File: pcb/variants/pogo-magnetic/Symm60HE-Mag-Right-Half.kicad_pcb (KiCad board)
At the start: 2 copper layers, 158.9 x 107.8 mm, 123 parts

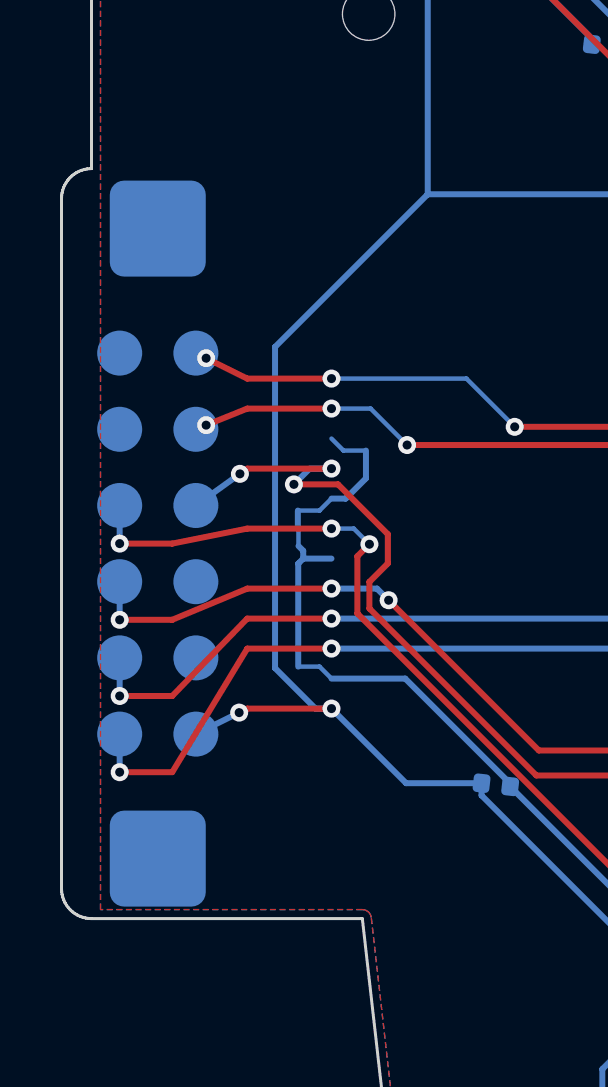
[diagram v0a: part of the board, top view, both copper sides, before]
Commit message: Survey the stocked magnetic pogo parts at twelve contacts and up
No manufacturer catalogue publishes a magnetic part above eight contacts, but
the ODM market does: single row on 2.54 mm goes to twenty, and dual row on
2.54 mm offers 8, 10, 12, 14 and 20 poles. Record the families with their
contact spans, since span is what decides whether a part fits the kernel.

A single-row twelve-contact part spans 27.94 mm, so about a 40 mm housing on a
47 mm module. The 2 x 6 dual row spans 12.70 mm on the 32 mm module this
variant already builds, which is why it wins despite the harder fanout.

Sixteen was tried: PER_ROW = 8 generates and routes but leaves three clearance
flags on the left half instead of two, so the crossing is the anchor geometry
rather than a shortage of slots, and it costs 5 mm of module length for four
spare grounds. Reverted to twelve.

Also move footprint generation into tools/make_mag_pogo_footprints.py so the
ICD constants drive the land pattern, and generalise the verifier's ground
count so either width checks.

Co-Authored-By: Claude Opus 5 <noreply@anthropic.com>
Claude-Session: https://claude.ai/code/session_01CRkZ4zVz5Mq7Fa3C5HAmii
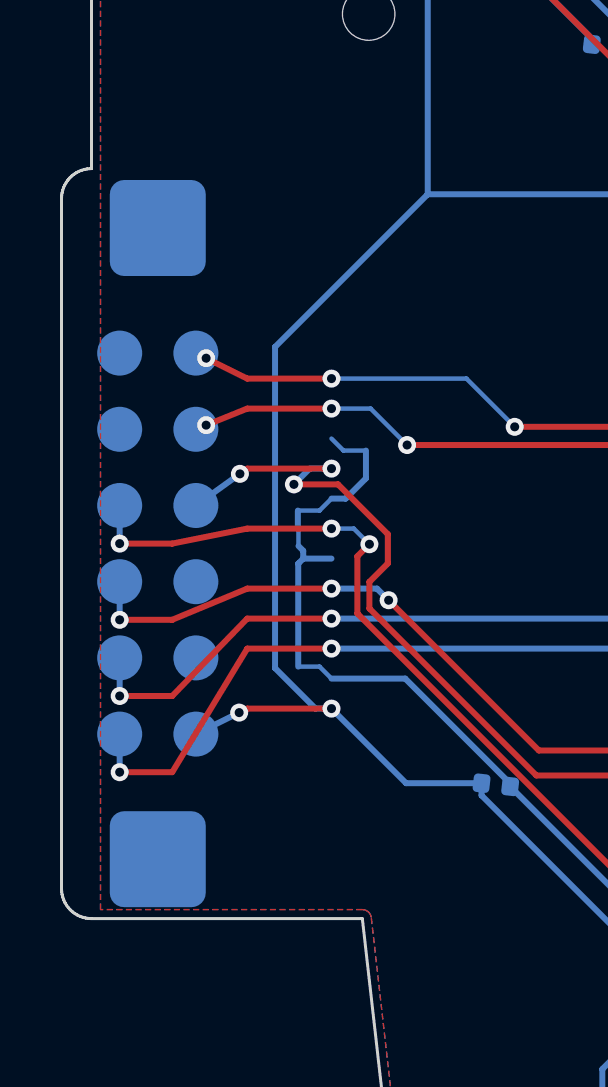
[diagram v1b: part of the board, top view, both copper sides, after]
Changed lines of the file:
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@@
 		(at 154.418 56 90)
 		(layer "B.Cu")
-		(descr "Magnetic pogo target half mating with MagPogo_2x6_P254_Spring. Built to ICD MAGPOGO-2x6-P254; confirm against the supplier drawing.")
+		(descr "Magnetic pogo target half mating with MagPogo_2x6_P254_Spring. Built to ICD MAGPOGO; confirm against the supplier drawing.")
 		(tags "magnetic pogo target 2x6 2.54mm")
 		(property
@@
 		(attr smd)
 		(fp_rect
-			(start -12.5 -4.5)
-			(end 12.5 4.5)
+			(start -12.52 -4.5)
+			(end 12.52 4.5)
 			(stroke
 				(width 0.12)
@@
 		)
 		(fp_rect
-			(start -13.0 -5.0)
-			(end 13.0 5.0)
+			(start -13.02 -5.0)
+			(end 13.02 5.0)
 			(stroke
 				(width 0.05)
@@
 		)
 		(fp_line
-			(start -12.5 -4.5)
-			(end 12.5 -4.5)
+			(start -12.52 -4.5)
+			(end 12.52 -4.5)
 			(stroke
 				(width 0.15)
@@
 			(layer "B.SilkS")
 		)
+		(fp_circle
+			(center -10.52 0)
+			(end -8.52 0)
+			(stroke
+				(width 0.12)
+				(type solid)
+			)
+			(fill none)
+			(layer "B.Fab")
+		)
 		(fp_line
-			(start -12.5 4.5)
-			(end 12.5 4.5)
+			(start -12.52 4.5)
+			(end 12.52 4.5)
 			(stroke
 				(width 0.15)
@@
 		)
 		(fp_circle
-			(center -10.5 0)
-			(end -8.5 0)
+			(center 10.52 0)
+			(end 12.52 0)
 			(stroke
 				(width 0.12)
@@
 		)
 		(fp_circle
-			(center 10.5 0)
-			(end 12.5 0)
-			(stroke
-				(width 0.12)
-				(type solid)
-			)
-			(fill none)
-			(layer "B.Fab")
-		)
-		(fp_circle
-			(center -6.35 2.77)
-			(end -6.05 -2.77)
+			(center -6.35 -0.22999999999999998)
+			(end -6.05 -0.22999999999999998)
 			(stroke
 				(width 0.15)
@@
 			smd
 			roundrect
-			(at -10.5 0)
+			(at -10.52 0)
 			(size 3.2 3.2)
 			(roundrect_rratio 0.15)
@@
 			smd
 			roundrect
-			(at 10.5 0)
+			(at 10.52 0)
 			(size 3.2 3.2)
 			(roundrect_rratio 0.15)
